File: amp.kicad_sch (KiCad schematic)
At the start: 18 parts, among them T1 BN-43-202, U2 RD16HHF1, U3 RD16HHF1

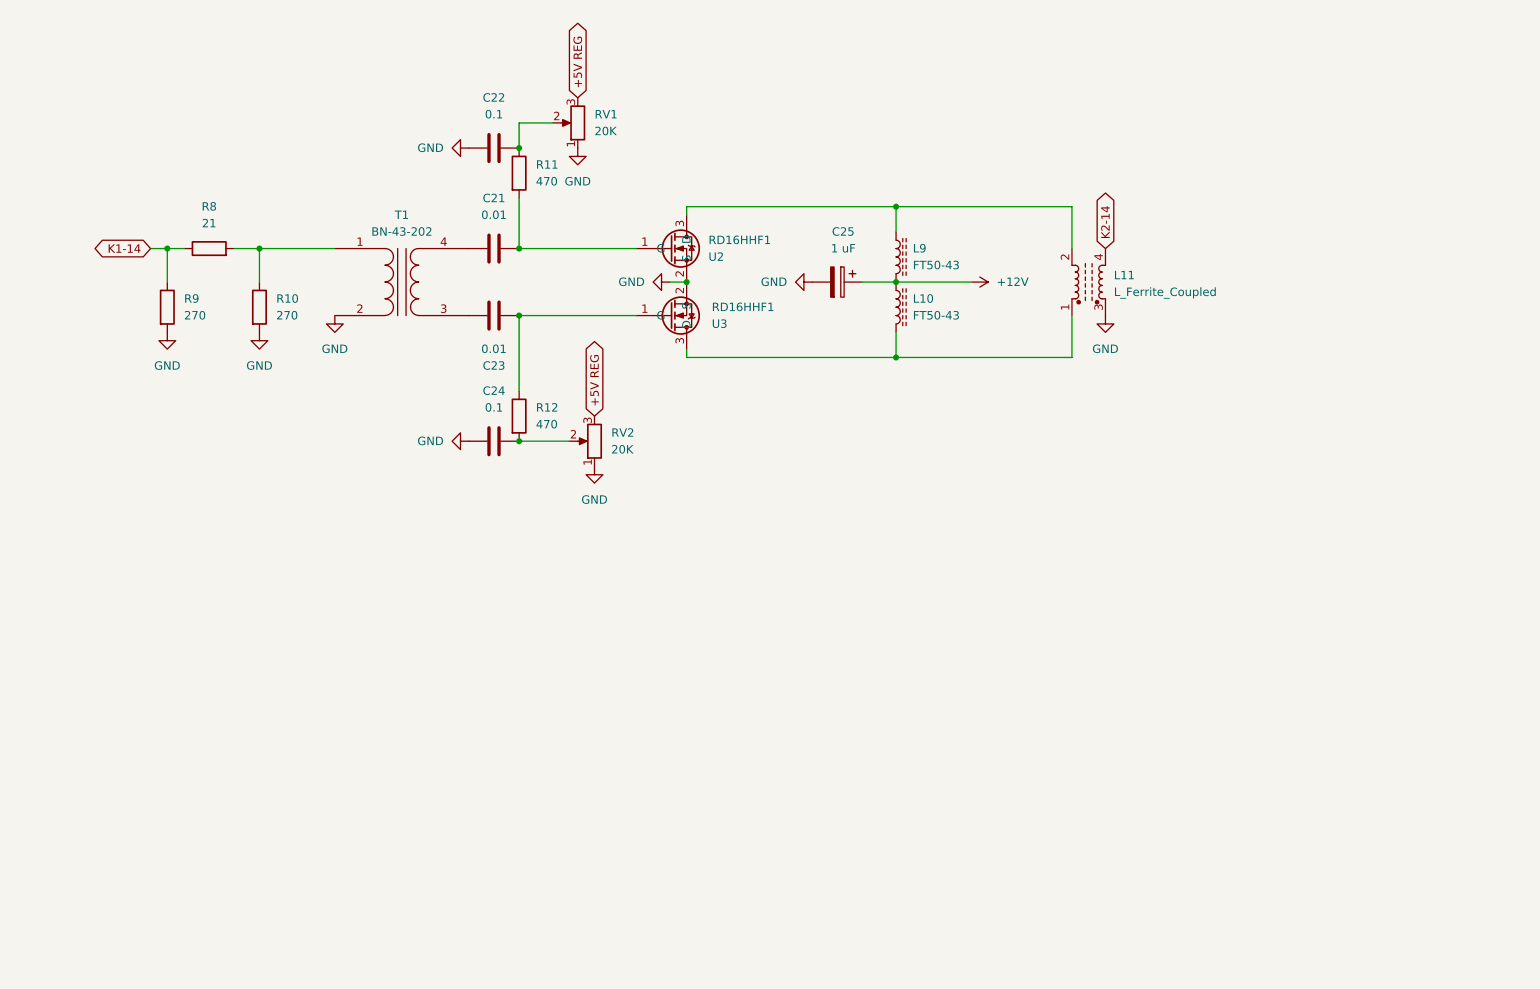
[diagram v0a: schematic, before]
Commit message: v0.6 ERC passes.  I went over it with a fine tooth comb and corrected lots of little stuff.  Ron should review all the components I have to create very carefully.  In particular, MPS-751 symbol does not look correct.
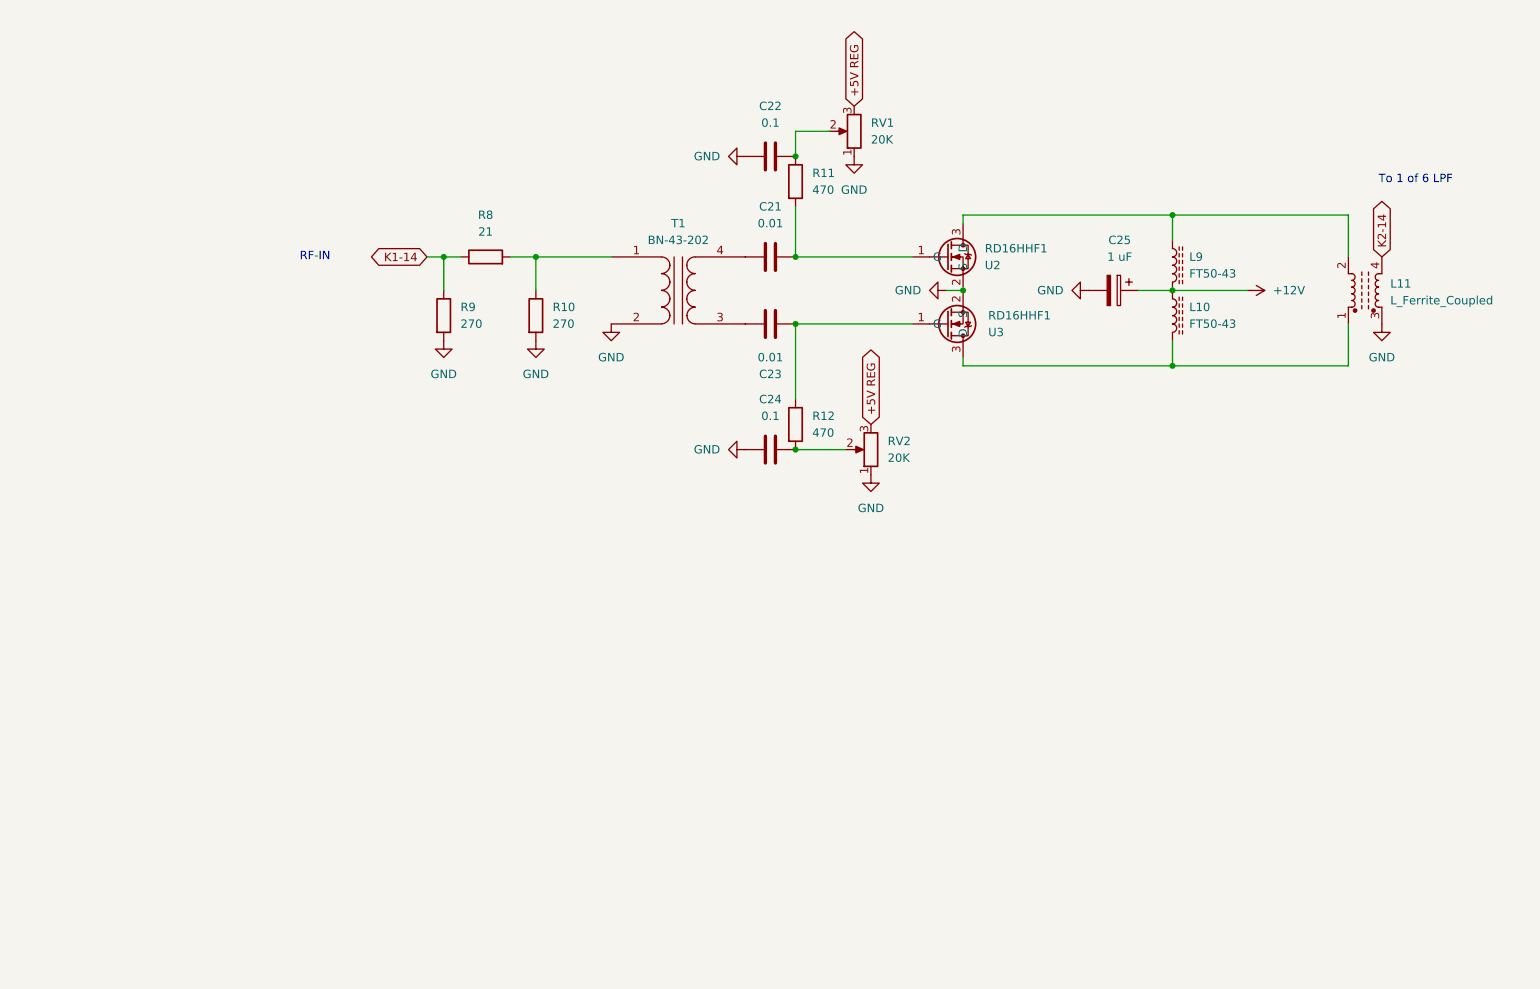
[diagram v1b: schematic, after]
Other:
- note added: "RF-IN"
- note added: "To 1 of 6 LPF"
- title: QMX Amp -> QMX+ Amp
- moved on the sheet: C21, C22, C23, C24, C25, L10, L11, L9, R10, R11, R12, R8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

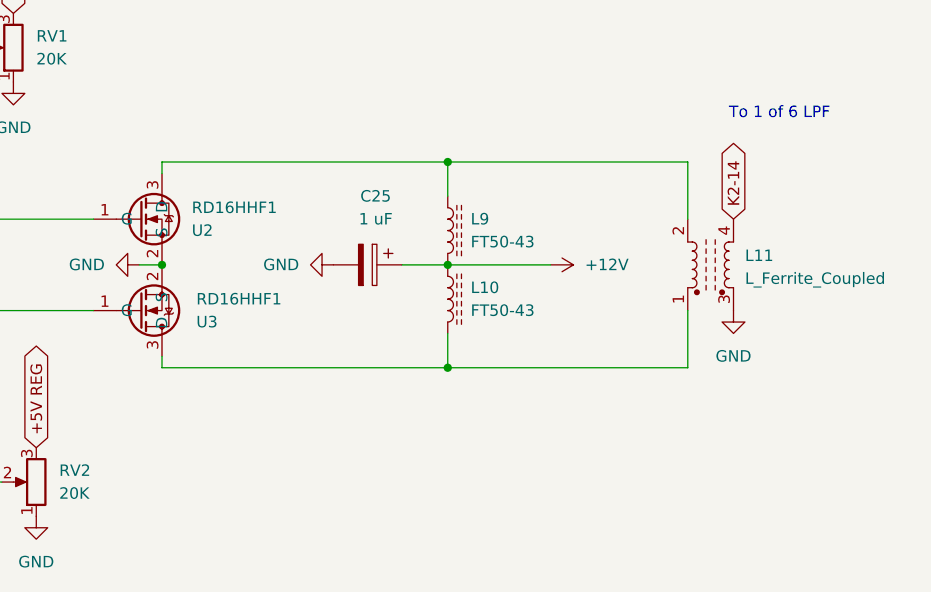
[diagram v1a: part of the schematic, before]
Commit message: v0.7 fixed MPS-751 and bifilar on FT50-43.  ERC passes
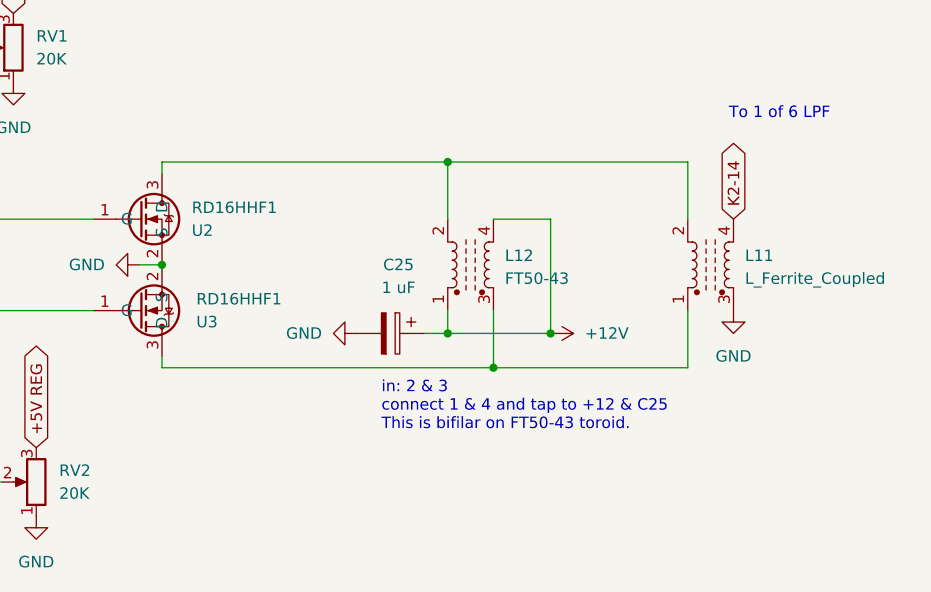
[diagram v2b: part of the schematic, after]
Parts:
- removed L10, L9: FT50-43, symbol Device:L_Ferrite
- added L12: FT50-43, symbol Device:L_Ferrite_Coupled
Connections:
- net +12V: now also L12.1, L12.4
- net at L11.2, U2.3 (D): now also L12.2
- net at L11.1, U3.3 (D): now also L12.3
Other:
- note added: "in: 2 & 3 connect 1 & 4 and tap to +12 & C25 This is bifilar on FT50-43 toroid."
- moved on the sheet: C25

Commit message: gave RD16HHF1 an TO-220 footprint
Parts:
- U2, U3: footprint Package_TO_SOT_THT:TO-220-3_Vertical -> Package_TO_SOT_THT:TO-220F-3_Horizontal_TabDown
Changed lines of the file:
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@@
 			)
 		)
-		(property "Footprint" "Package_TO_SOT_THT:TO-220-3_Vertical"
+		(property "Footprint" "Package_TO_SOT_THT:TO-220F-3_Horizontal_TabDown"
 			(at 158.75 100.33 0)
 			(effects
@@
 			)
 		)
-		(property "Footprint" "Package_TO_SOT_THT:TO-220-3_Vertical"
+		(property "Footprint" "Package_TO_SOT_THT:TO-220F-3_Horizontal_TabDown"
 			(at 158.75 77.47 0)
 			(effects

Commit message: I think I am working on picking parts
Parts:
- L11: value L_Ferrite_Coupled -> BN-43-7051; footprint (none) -> ZZZMyLibrary:BN-43-202-FLAT
- L12: footprint (none) -> ZZZMyLibrary:Toroid_T50_Vertical_L14.0mm_W5.6mm_4pins
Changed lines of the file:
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@@
 			)
 		)
-		(property "Value" "L_Ferrite_Coupled"
+		(property "Value" "BN-43-7051"
 			(at 226.06 90.4239 90)
 			(effects
@@
 			)
 		)
-		(property "Footprint" ""
+		(property "Footprint" "ZZZMyLibrary:BN-43-202-FLAT"
 			(at 222.25 88.9 0)
 			(effects
@@
 			)
 		)
-		(property "Footprint" ""
+		(property "Footprint" "ZZZMyLibrary:Toroid_T50_Vertical_L14.0mm_W5.6mm_4pins"
 			(at 195.58 88.9 0)
 			(effects

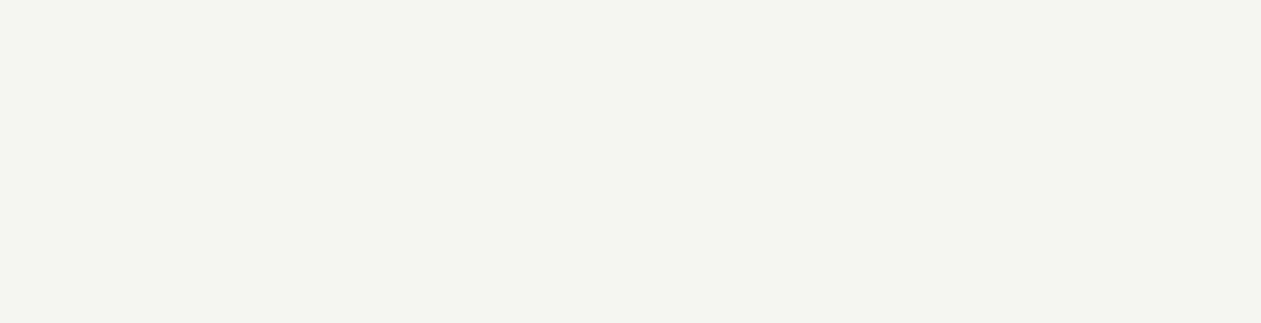
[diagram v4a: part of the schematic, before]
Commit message: created 11x4mm footprint with 5mm pin spacing for caps on LPF per Ron
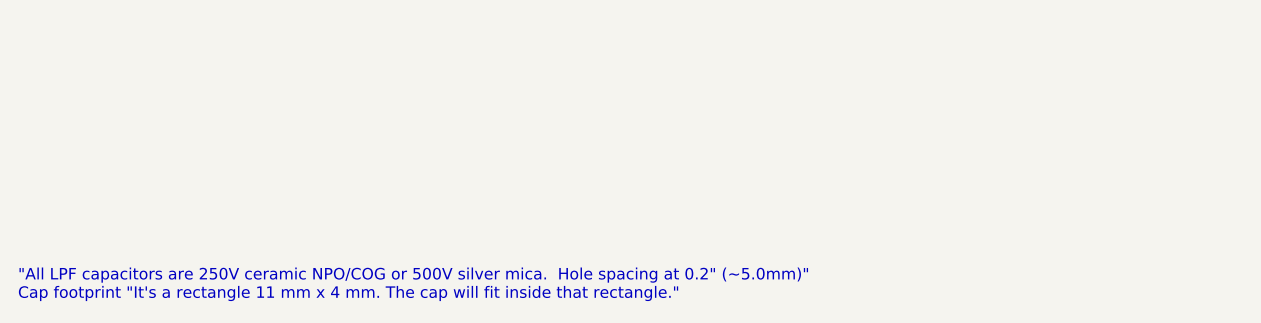
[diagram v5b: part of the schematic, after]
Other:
- note added: ""All LPF capacitors are 250V ceramic NPO/COG or 500V silver mica. Hole spacing at 0.2" (~5.0mm)" Cap footprint "It's a rectangle 11 mm x 4 mm. The cap will fit inside that rectangle.""
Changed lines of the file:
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@@
 	(title_block
 		(title "QMX+ Amp")
-		(date "2024-08-13")
+		(date "2024-08-18")
 		(rev "v0.7")
 		(company "WA7GIL")
@@
 		(effects
 			(font
+				(size 1.27 1.27)
+			)
+			(justify left)
+		)
+	)
+	(text "\"All LPF capacitors are 250V ceramic NPO/COG or 500V silver mica.  Hole spacing at 0.2\" (~5.0mm)\"\nCap footprint \"It's a rectangle 11 mm x 4 mm. The cap will fit inside that rectangle.\""
+		(exclude_from_sim no)
+		(at 17.272 190.754 0)
+		(effects
+			(font

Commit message: ron came by and gave lots of feedback.  many notes on schematic for additional changes
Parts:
- C21, C22, C23, C24, C25: footprint (none) -> ZZZMyLibrary:C_Disc_D11.0mm_W4.0mm_P5.00mm
- R10, R11, R12, R8, R9, RV1, RV2: footprint (none) -> Resistor_THT:R_Axial_DIN0309_L9.0mm_D3.2mm_P12.70mm_Horizontal
- T1: footprint (none) -> ZZZMyLibrary:BN-43-202-FLAT
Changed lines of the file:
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@@
 			)
 		)
-		(property "Footprint" ""
+		(property "Footprint" "Resistor_THT:R_Axial_DIN0309_L9.0mm_D3.2mm_P12.70mm_Horizontal"
 			(at 144.78 64.77 0)
 			(effects
@@
 			)
 		)
-		(property "Footprint" ""
+		(property "Footprint" "Resistor_THT:R_Axial_DIN0309_L9.0mm_D3.2mm_P12.70mm_Horizontal"
 			(at 80.772 92.71 90)
 			(effects
@@
 			)
 		)
-		(property "Footprint" ""
+		(property "Footprint" "ZZZMyLibrary:C_Disc_D11.0mm_W4.0mm_P5.00mm"
 			(at 182.88 97.4852 0)
 			(effects
@@
 			)
 		)
-		(property "Footprint" ""
+		(property "Footprint" "ZZZMyLibrary:BN-43-202-FLAT"
 			(at 118.11 88.9 0)
 			(effects
@@
 			)
 		)
-		(property "Footprint" ""
+		(property "Footprint" "ZZZMyLibrary:C_Disc_D11.0mm_W4.0mm_P5.00mm"
 			(at 135.89 112.0648 0)
 			(effects
@@
 			)
 		)
-		(property "Footprint" ""
+		(property "Footprint" "Resistor_THT:R_Axial_DIN0309_L9.0mm_D3.2mm_P12.70mm_Horizontal"
 			(at 147.32 113.03 0)
 			(effects
@@
 			)
 		)
-		(property "Footprint" ""
+		(property "Footprint" "ZZZMyLibrary:C_Disc_D11.0mm_W4.0mm_P5.00mm"
 			(at 135.89 67.6148 0)
 			(effects
@@
 			)
 		)
-		(property "Footprint" ""
+		(property "Footprint" "ZZZMyLibrary:C_Disc_D11.0mm_W4.0mm_P5.00mm"
 			(at 135.89 82.8548 0)
 			(effects
@@
 			)
 		)
-		(property "Footprint" ""
+		(property "Footprint" "Resistor_THT:R_Axial_DIN0309_L9.0mm_D3.2mm_P12.70mm_Horizontal"
 			(at 134.112 109.22 90)
 			(effects
@@
 			)
 		)
-		(property "Footprint" ""
+		(property "Footprint" "Resistor_THT:R_Axial_DIN0309_L9.0mm_D3.2mm_P12.70mm_Horizontal"
 			(at 134.112 72.39 90)
 			(effects
@@
 			)
 		)
-		(property "Footprint" ""
+		(property "Footprint" "ZZZMyLibrary:C_Disc_D11.0mm_W4.0mm_P5.00mm"
 			(at 135.89 94.9452 0)
 			(effects
@@
 			)
 		)
-		(property "Footprint" ""
+		(property "Footprint" "Resistor_THT:R_Axial_DIN0309_L9.0mm_D3.2mm_P12.70mm_Horizontal"
 			(at 88.9 85.598 90)
 			(effects
@@
 			)
 		)
-		(property "Footprint" ""
+		(property "Footprint" "Resistor_THT:R_Axial_DIN0309_L9.0mm_D3.2mm_P12.70mm_Horizontal"
 			(at 94.742 92.71 90)
 			(effects

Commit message: expended to all 6 LPFs.  ERC pass.  Need to check component values on new LPF page
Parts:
- renumbered C22 to C21, C21 to C22, L11 to L10, L12 to L9, R9 to R8, R8 to R9, U2 to U3, U3 to U4
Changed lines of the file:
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@@
 		(dnp no)
 		(fields_autoplaced yes)
-		(property "Reference" "#PWR044"
+		(property "Reference" "#PWR048"
 			(at 176.53 96.52 0)
 			(effects
@@
 			(project ""
 				(path "/e63e39d7-6ac0-4ffd-8aa3-1841a4541b55/768704d5-e7b1-4c2a-9d2e-06c065a4fa64"
-					(reference "#PWR044")
+					(reference "#PWR048")
 					(unit 1)
 				)
@@
 		(dnp no)
 		(fields_autoplaced yes)
-		(property "Reference" "R9"
+		(property "Reference" "R8"
 			(at 85.09 91.4399 0)
 			(effects
@@
 			(project ""
 				(path "/e63e39d7-6ac0-4ffd-8aa3-1841a4541b55/768704d5-e7b1-4c2a-9d2e-06c065a4fa64"
-					(reference "R9")
+					(reference "R8")
 					(unit 1)
 				)
@@
 		(dnp no)
 		(fields_autoplaced yes)
-		(property "Reference" "#PWR045"
+		(property "Reference" "#PWR050"
 			(at 224.79 100.33 0)
 			(effects
@@
 			(project "QMX-amp"
 				(path "/e63e39d7-6ac0-4ffd-8aa3-1841a4541b55/768704d5-e7b1-4c2a-9d2e-06c065a4fa64"
-					(reference "#PWR045")
+					(reference "#PWR050")
 					(unit 1)
 				)
@@
 		(dnp no)
 		(fields_autoplaced yes)
-		(property "Reference" "L11"
+		(property "Reference" "L10"
 			(at 226.06 87.8839 90)
 			(effects
@@
 			(project ""
 				(path "/e63e39d7-6ac0-4ffd-8aa3-1841a4541b55/768704d5-e7b1-4c2a-9d2e-06c065a4fa64"
-					(reference "L11")
+					(reference "L10")
 					(unit 1)
 				)
@@
 		(dnp no)
 		(fields_autoplaced yes)
-		(property "Reference" "#PWR043"
+		(property "Reference" "#PWR049"
 			(at 200.66 96.52 0)
 			(effects
@@
 			(project ""
 				(path "/e63e39d7-6ac0-4ffd-8aa3-1841a4541b55/768704d5-e7b1-4c2a-9d2e-06c065a4fa64"
-					(reference "#PWR043")
+					(reference "#PWR049")
 					(unit 1)
 				)
@@
 		(dnp no)
 		(fields_autoplaced yes)
-		(property "Reference" "#PWR038"
+		(property "Reference" "#PWR045"
 			(at 144.78 74.93 0)
 			(effects
@@
 			(project "QMX-amp"
 				(path "/e63e39d7-6ac0-4ffd-8aa3-1841a4541b55/768704d5-e7b1-4c2a-9d2e-06c065a4fa64"
-					(reference "#PWR038")
+					(reference "#PWR045")
 					(unit 1)
 				)
@@
 		(on_board yes)
 		(dnp no)
-		(property "Reference" "U3"
+		(property "Reference" "U4"
 			(at 165.1 95.2501 0)
 			(effects
@@
 			(project "QMX-amp"
 				(path "/e63e39d7-6ac0-4ffd-8aa3-1841a4541b55/768704d5-e7b1-4c2a-9d2e-06c065a4fa64"
-					(reference "U3")
+					(reference "U4")
 					(unit 1)
 				)
@@
 		(dnp no)
 		(fields_autoplaced yes)
-		(property "Reference" "#PWR036"
+		(property "Reference" "#PWR042"
 			(at 107.95 100.33 0)
 			(effects
@@
 			(project ""
 				(path "/e63e39d7-6ac0-4ffd-8aa3-1841a4541b55/768704d5-e7b1-4c2a-9d2e-06c065a4fa64"
-					(reference "#PWR036")
+					(reference "#PWR042")
 					(unit 1)
 				)
@@
 		(dnp no)
 		(fields_autoplaced yes)
-		(property "Reference" "#PWR037"
+		(property "Reference" "#PWR043"
 			(at 121.92 68.58 0)
 			(effects
@@
 			(project "QMX-amp"
 				(path "/e63e39d7-6ac0-4ffd-8aa3-1841a4541b55/768704d5-e7b1-4c2a-9d2e-06c065a4fa64"
-					(reference "#PWR037")
+					(reference "#PWR043")
 					(unit 1)
 				)
@@
 		(dnp no)
 		(fields_autoplaced yes)
-		(property "Reference" "#PWR035"
+		(property "Reference" "#PWR041"
 			(at 96.52 102.87 0)
 			(effects
@@
 			(project ""
 				(path "/e63e39d7-6ac0-4ffd-8aa3-1841a4541b55/768704d5-e7b1-4c2a-9d2e-06c065a4fa64"
-					(reference "#PWR035")
+					(reference "#PWR041")
 					(unit 1)
 				)
@@
 		(dnp no)
 		(fields_autoplaced yes)
-		(property "Reference" "C22"
+		(property "Reference" "C21"
 			(at 132.08 60.96 90)
 			(effects
@@
 			(project ""
 				(path "/e63e39d7-6ac0-4ffd-8aa3-1841a4541b55/768704d5-e7b1-4c2a-9d2e-06c065a4fa64"
-					(reference "C22")
+					(reference "C21")
 					(unit 1)
 				)
@@
 		(dnp no)
 		(fields_autoplaced yes)
-		(property "Reference" "L12"
+		(property "Reference" "L9"
 			(at 199.39 87.8839 90)
 			(effects
@@
 			(project "QMX-amp"
 				(path "/e63e39d7-6ac0-4ffd-8aa3-1841a4541b55/768704d5-e7b1-4c2a-9d2e-06c065a4fa64"
-					(reference "L12")
+					(reference "L9")
 					(unit 1)
 				)
@@
 		(dnp no)
 		(fields_autoplaced yes)
-		(property "Reference" "#PWR041"
+		(property "Reference" "#PWR047"
 			(at 152.4 88.9 0)
 			(effects
@@
 			(project ""
 				(path "/e63e39d7-6ac0-4ffd-8aa3-1841a4541b55/768704d5-e7b1-4c2a-9d2e-06c065a4fa64"
-					(reference "#PWR041")
+					(reference "#PWR047")
 					(unit 1)
 				)
@@
 		(dnp no)
 		(fields_autoplaced yes)
-		(property "Reference" "C21"
+		(property "Reference" "C22"
 			(at 132.08 76.2 90)
 			(effects
@@
 			(project ""
 				(path "/e63e39d7-6ac0-4ffd-8aa3-1841a4541b55/768704d5-e7b1-4c2a-9d2e-06c065a4fa64"
-					(reference "C21")
+					(reference "C22")
 					(unit 1)
 				)
@@
 		(on_board yes)
 		(dnp no)
-		(property "Reference" "U2"
+		(property "Reference" "U3"
 			(at 164.592 85.09 0)
 			(effects
@@
 			(project ""
 				(path "/e63e39d7-6ac0-4ffd-8aa3-1841a4541b55/768704d5-e7b1-4c2a-9d2e-06c065a4fa64"
-					(reference "U2")
+					(reference "U3")
 					(unit 1)
 				)
@@
 		(dnp no)
 		(fields_autoplaced yes)
-		(property "Reference" "R8"
+		(property "Reference" "R9"
 			(at 88.9 77.47 90)
 			(effects
@@
 			(project ""
 				(path "/e63e39d7-6ac0-4ffd-8aa3-1841a4541b55/768704d5-e7b1-4c2a-9d2e-06c065a4fa64"
-					(reference "R8")
+					(reference "R9")
 					(unit 1)
 				)
@@
 		(dnp no)
 		(fields_autoplaced yes)
-		(property "Reference" "#PWR034"
+		(property "Reference" "#PWR040"
 			(at 82.55 102.87 0)
 			(effects
@@
 			(project ""
 				(path "/e63e39d7-6ac0-4ffd-8aa3-1841a4541b55/768704d5-e7b1-4c2a-9d2e-06c065a4fa64"
-					(reference "#PWR034")
+					(reference "#PWR040")
 					(unit 1)
 				)
@@
 		(dnp no)
 		(fields_autoplaced yes)
-		(property "Reference" "#PWR039"
+		(property "Reference" "#PWR044"
 			(at 121.92 113.03 0)
 			(effects
@@
 			(project "QMX-amp"
 				(path "/e63e39d7-6ac0-4ffd-8aa3-1841a4541b55/768704d5-e7b1-4c2a-9d2e-06c065a4fa64"
-					(reference "#PWR039")
+					(reference "#PWR044")
 					(unit 1)
 				)
@@
 		(dnp no)
 		(fields_autoplaced yes)
-		(property "Reference" "#PWR040"
+		(property "Reference" "#PWR046"
 			(at 147.32 123.19 0)
 			(effects
@@
 			(project "QMX-amp"
 				(path "/e63e39d7-6ac0-4ffd-8aa3-1841a4541b55/768704d5-e7b1-4c2a-9d2e-06c065a4fa64"
-					(reference "#PWR040")
-					(unit 1)
-				)
+					(reference "#PWR046")
+					(unit 1)
+				)
